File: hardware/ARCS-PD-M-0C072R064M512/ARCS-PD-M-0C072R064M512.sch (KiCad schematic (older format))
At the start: 0 parts

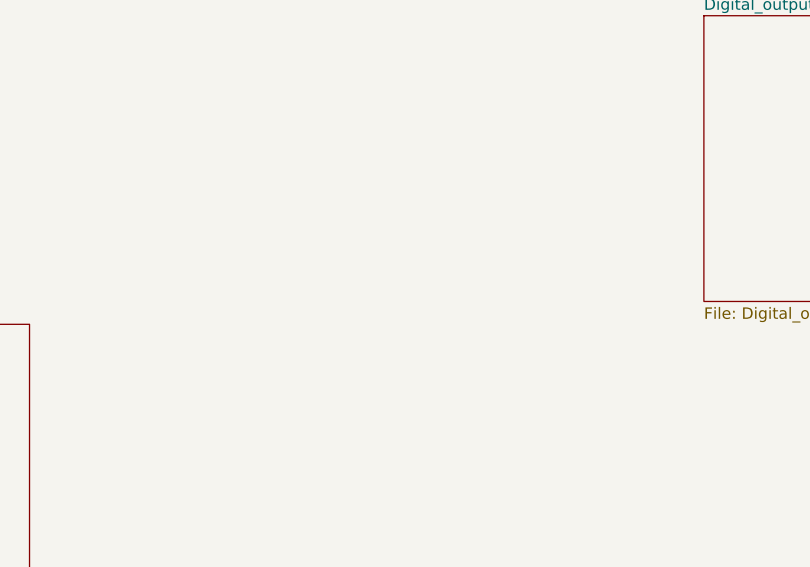
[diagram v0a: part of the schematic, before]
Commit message: Create cards for input and output interface.
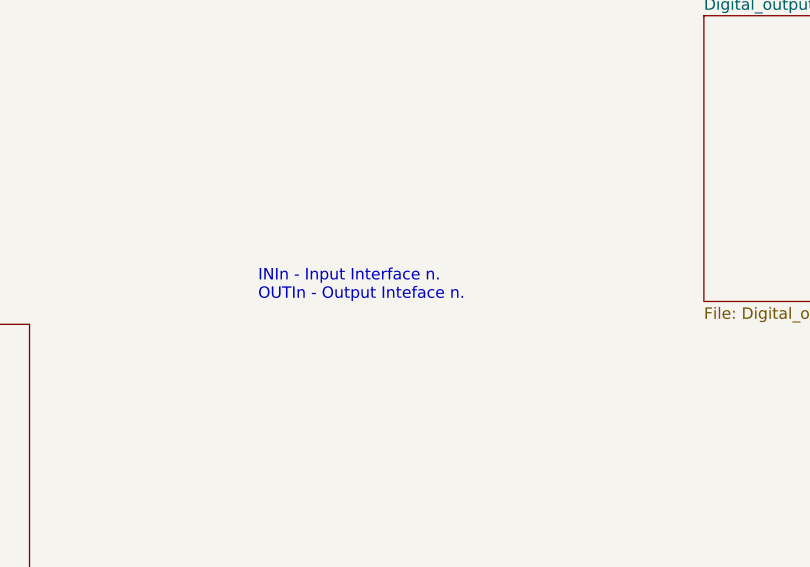
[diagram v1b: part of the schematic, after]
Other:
- note added: "INIn - Input Interface n.\nOUTIn - Output Inteface n."
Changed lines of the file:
@@
 F1 "Ethernet_W5100.sch" 50
 $EndSheet
+Text Notes 6950 6200 0    50   ~ 0
+INIn - Input Interface n.\nOUTIn - Output Inteface n.
 $EndSCHEMATC
